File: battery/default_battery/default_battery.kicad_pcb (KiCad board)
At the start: 2 copper layers, 14 parts

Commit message: update battery module
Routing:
- net VBAT: track 31.0 -> 32.6 mm, vias 0 -> 1
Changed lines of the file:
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@@
 	)
 	(segment
-		(start -4.669 -35.494)
-		(end 1.874 -35.494)
-		(width 0.2)
-		(layer "F.Cu")
-		(net 1)
-	)
-	(segment
-		(start -5.175 -36)
-		(end -4.669 -35.494)
+		(start -5.175 -34.765)
+		(end -5.18 -34.76)
 		(width 0.2)
 		(layer "F.Cu")
@@
 	)
 	(segment
+		(start -5.175 -36)
+		(end -5.175 -34.765)
+		(width 0.2)
+		(layer "F.Cu")
+		(net 1)
+	)
+	(segment
 		(start 0 -26.54)
 		(end 2.54 -24)
@@
 		(net 1)
 	)
+	(via
+		(at -5.18 -34.76)
+		(size 0.6)
+		(drill 0.3)
+		(layers "F.Cu" "B.Cu")
+		(net 1)
+	)
+	(segment
+		(start 0 -33.64)
+		(end -1.12 -34.76)
+		(width 0.2)
+		(layer "B.Cu")
+		(net 1)
+	)
+	(segment
+		(start -1.12 -34.76)
+		(end -5.18 -34.76)
+		(width 0.2)
+		(layer "B.Cu")
+		(net 1)
+	)
+	(segment
+		(start 0 -31.62)
+		(end 0 -33.64)
+		(width 0.2)
+		(layer "B.Cu")
+		(net 1)
+	)

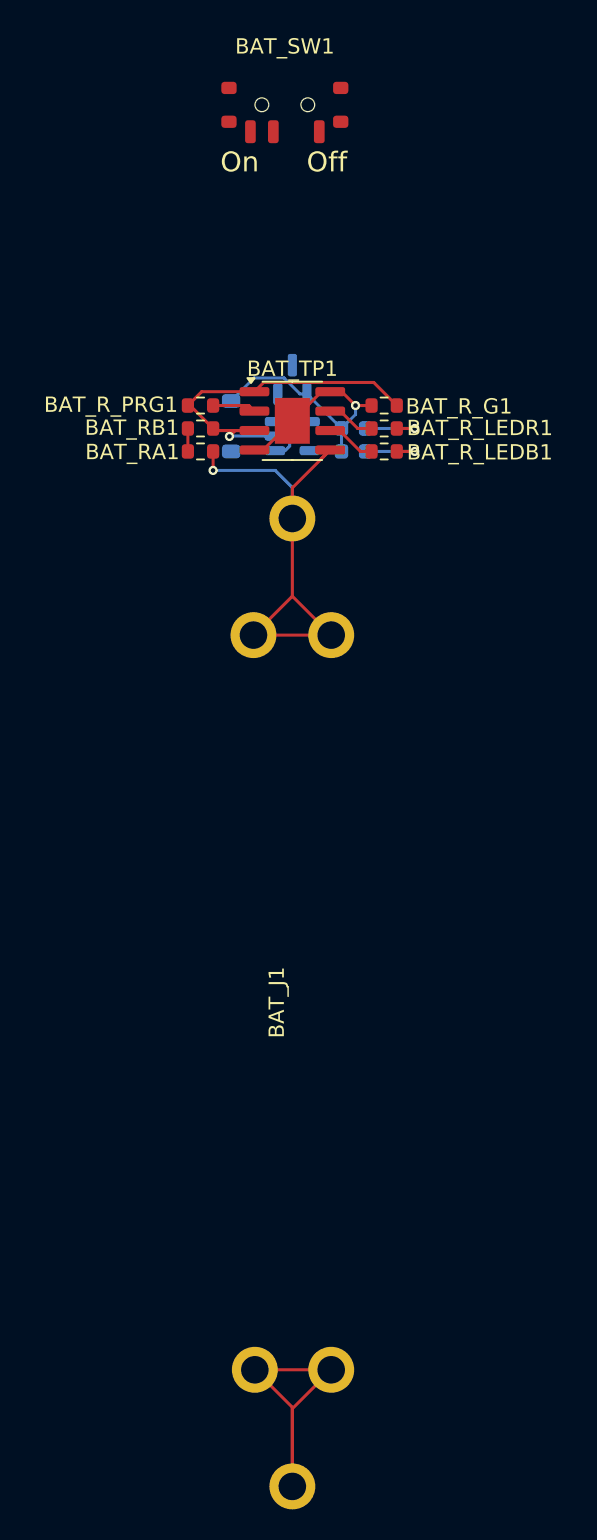
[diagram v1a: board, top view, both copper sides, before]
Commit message: update battery module, change switch
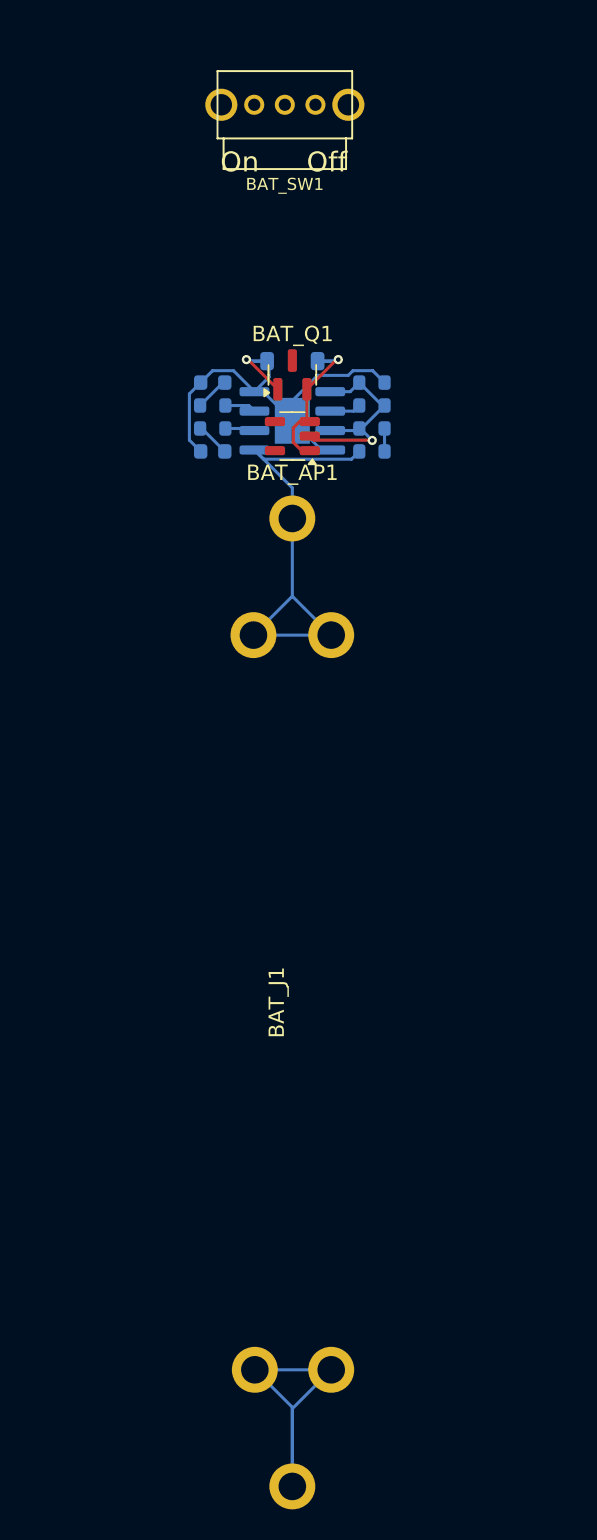
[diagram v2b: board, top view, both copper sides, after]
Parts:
- BAT_AP1, BAT_Q1: moved to F.Cu
- BAT_RA1, BAT_RB1, BAT_R_G1, BAT_R_LEDB1, BAT_R_LEDR1, BAT_R_PRG1, BAT_TP1: moved to B.Cu
- BAT_SW1: footprint ErgoCai.pretty:MSK-12C02 -> ErgoCai.pretty:SK12D07VG4
- moved BAT_R_LEDB1 11.3 mm to (-5.20, -37.5), turned to 0 degrees
- moved BAT_R_LEDR1 11.3 mm to (-5.20, -39.0), turned to 0 degrees
- moved BAT_RA1 11.2 mm to (5.20, -36.0), turned to 0 degrees
- moved BAT_RB1 11.2 mm to (5.20, -37.5), turned to 180 degrees
- moved BAT_R_PRG1 11.2 mm to (5.20, -39.0), turned to 0 degrees
- moved BAT_LEDR1 9.68 mm to (-5.20, -40.5)
- moved BAT_LEDB1 9.20 mm to (-5.20, -36.0)
- moved BAT_D1 5.84 mm to (0.00, -41.9), turned to 180 degrees
- moved BAT_R_G1 1.70 mm to (5.20, -40.5), turned to 180 degrees
- moved BAT_Q1 0.30 mm to (0.00, -41.0)
- turned BAT_AP1 to 180 degrees
- turned BAT_TP1 to 180 degrees
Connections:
- BAT_SW1 pad 1: unconnected-(BAT_SW1A-A-Pad1) -> Net-(BAT_Q1-D)
- BAT_SW1 pad 2: VBAT -> unconnected-(BAT_SW1-Pad2)
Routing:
- net GND: track 46.9 -> 36.4 mm
- net VBUS: track 23.0 -> 32.4 mm
- net Net-(BAT_AP1-EN): track 8.07 -> 11.2 mm, vias 0 -> 1
- net VBAT: track 32.6 -> 30.2 mm, vias 1 -> 0
- net Net-(BAT_LEDB1-K): track 4.45 -> 2.23 mm, vias 1 -> 0
- net Net-(BAT_LEDR1-K): track 4.44 -> 2.23 mm, vias 1 -> 0
- net Net-(BAT_TP1-~{STDBY}): track 3.07 -> 1.96 mm
- net Net-(BAT_TP1-~{CHRG}): track 2.97 -> 2.05 mm
- net Net-(BAT_TP1-PROG): track 2.65 -> 2.05 mm

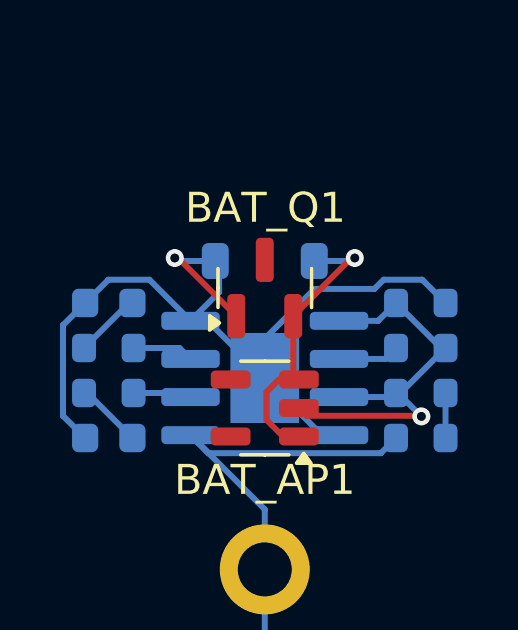
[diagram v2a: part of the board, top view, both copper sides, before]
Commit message: update battery module, update via pos
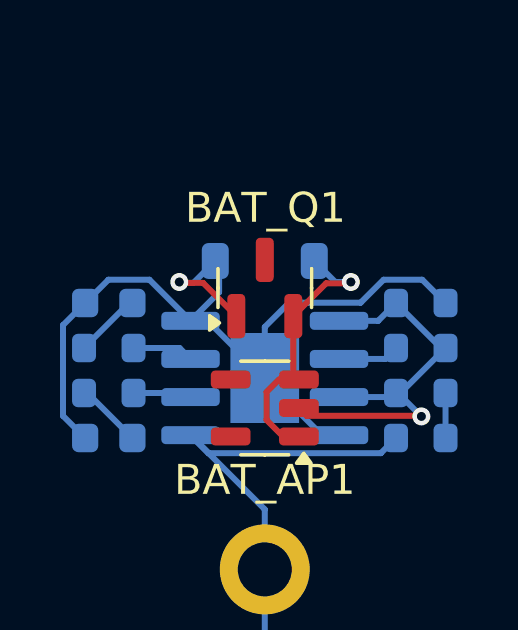
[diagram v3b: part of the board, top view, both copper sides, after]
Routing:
- net Net-(BAT_AP1-EN): track 11.2 -> 9.53 mm
- net VBUS: track 32.4 -> 30.9 mm
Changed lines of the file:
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@@
 	)
 	(segment
-		(start -2.8875 -42)
-		(end -3 -42)
+		(start -2.0575 -41.17)
+		(end -2.81 -41.17)
 		(width 0.2)
 		(layer "F.Cu")
@@
 	(segment
 		(start -0.95 -40.0625)
-		(end -2.8875 -42)
+		(end -2.0575 -41.17)
 		(width 0.2)
 		(layer "F.Cu")
@@
 	)
 	(via
-		(at -3 -42)
+		(at -2.85 -41.2)
 		(size 0.6)
 		(drill 0.3)
@@
 	)
 	(segment
+		(start -1.65 -41.9)
+		(end -2.38 -41.17)
+		(width 0.2)
+		(layer "B.Cu")
+		(net 4)
+	)
+	(segment
+		(start 3.961936 -41.276)
+		(end 5.249 -41.276)
+		(width 0.2)
+		(layer "B.Cu")
+		(net 4)
+	)
+	(segment
 		(start -6.726 -36.7385)
 		(end -6.726 -39.7615)
@@
 	)
 	(segment
-		(start -2.91 -41.9)
-		(end -2.92 -41.91)
-		(width 0.2)
-		(layer "B.Cu")
-		(net 4)
-	)
-	(segment
 		(start -5.9875 -36)
 		(end -6.726 -36.7385)
@@
 	)
 	(segment
-		(start 0 -39.310761)
-		(end 1.658239 -40.969)
+		(start 3.195936 -40.51)
+		(end 3.961936 -41.276)
 		(width 0.2)
 		(layer "B.Cu")
@@
 	)
 	(segment
+		(start 0 -38)
+		(end 0 -39.7)
+		(width 0.2)
+		(layer "B.Cu")
+		(net 4)
+	)
+	(segment
 		(start -5.2115 -41.276)
 		(end -3.846 -41.276)
@@
 	)
 	(segment
+		(start 5.249 -41.276)
+		(end 6.025 -40.5)
+		(width 0.2)
+		(layer "B.Cu")
+		(net 4)
+	)
+	(segment
 		(start -6.726 -39.7615)
 		(end -5.9875 -40.5)
@@
 	)
 	(segment
-		(start 3.654936 -40.969)
-		(end 3.961936 -41.276)
-		(width 0.2)
-		(layer "B.Cu")
-		(net 4)
-	)
-	(segment
-		(start -2.9 -41.9)
-		(end -3 -42)
+		(start 0 -39.7)
+		(end 0.81 -40.51)
 		(width 0.2)
 		(layer "B.Cu")
@@
 	)
 	(segment
-		(start -1.65 -41.9)
-		(end -2.9 -41.9)
-		(width 0.2)
-		(layer "B.Cu")
-		(net 4)
-	)
-	(segment
 		(start -1.5225 -40.8575)
 		(end -1.5225 -41.87)
@@
 	)
 	(segment
-		(start 3.961936 -41.276)
-		(end 5.249 -41.276)
-		(width 0.2)
-		(layer "B.Cu")
-		(net 4)
-	)
-	(segment
 		(start 0 -38)
 		(end 1.905 -36.095)
@@
 	)
 	(segment
-		(start -2.73 -41.9)
-		(end -2.91 -41.9)
-		(width 0.2)
-		(layer "B.Cu")
-		(net 4)
-	)
-	(segment
-		(start 5.249 -41.276)
-		(end 6.025 -40.5)
-		(width 0.2)
-		(layer "B.Cu")
-		(net 4)
-	)
-	(segment
 		(start -5.9875 -40.5)
 		(end -5.2115 -41.276)
@@
 	)
 	(segment
-		(start -1.65 -41.9)
-		(end -2.73 -41.9)
-		(width 0.2)
-		(layer "B.Cu")
-		(net 4)
-	)
-	(segment
-		(start 1.658239 -40.969)
-		(end 3.654936 -40.969)
-		(width 0.2)
-		(layer "B.Cu")
-		(net 4)
-	)
-	(segment
-		(start 0 -38)
-		(end 0 -39.310761)
-		(width 0.2)
-		(layer "B.Cu")
-		(net 4)
-	)
-	(segment
-		(start 2.8875 -42)
-		(end 3 -42)
+		(start 0.81 -40.51)
+		(end 3.195936 -40.51)
+		(width 0.2)
+		(layer "B.Cu")
+		(net 4)
+	)
+	(segment
+		(start -2.38 -41.17)
+		(end -2.81 -41.17)
+		(width 0.2)
+		(layer "B.Cu")
+		(net 4)
+	)
+	(segment
+		(start 0.95 -40.0625)
+		(end 2.0435 -41.156)
 		(width 0.2)
 		(layer "F.Cu")
@@
 	)
 	(segment
+		(start 2.0435 -41.156)
+		(end 2.84 -41.156)
+		(width 0.2)
+		(layer "F.Cu")
+		(net 7)
+	)
+	(segment
 		(start 0.61 -36.05)
 		(end 1.1375 -36.05)
@@
 		(net 7)
 	)
-	(segment
-		(start 0.95 -40.0625)
-		(end 2.8875 -42)
-		(width 0.2)
-		(layer "F.Cu")
-		(net 7)
-	)
 	(via
-		(at 3 -42)
+		(at 2.87 -41.2)
 		(size 0.6)
 		(drill 0.3)
@@
 	)
 	(segment
-		(start 1.65 -41.9)
-		(end 2.9 -41.9)
-		(width 0.2)
-		(layer "B.Cu")
-		(net 7)
-	)
-	(segment
-		(start 2.9 -41.9)
-		(end 3 -42)
-		(width 0.2)
-		(layer "B.Cu")
-		(net 7)
-	)
-	(segment
-		(start 2.8 -41.9)
-		(end 2.81 -41.91)
-		(width 0.2)
-		(layer "B.Cu")
-		(net 7)
-	)
-	(segment
-		(start 2.81 -41.91)
-		(end 2.93 -41.91)
-		(width 0.2)
-		(layer "B.Cu")
-		(net 7)
-	)
-	(segment
-		(start 1.65 -41.9)
-		(end 2.8 -41.9)
-		(width 0.2)
-		(layer "B.Cu")
-		(net 7)
-	)
-	(segment
-		(start 2.93 -41.91)
-		(end 2.94 -41.92)
-		(width 0.2)
-		(layer "B.Cu")
+		(start 2.87 -41.2)
+		(end 2.35 -41.2)
+		(width 0.2)
+		(layer "B.Cu")
+		(net 7)
+	)
+	(segment
+		(start 2.35 -41.2)
+		(end 1.65 -41.9)
+		(width 0.2)
+		(layer "B.Cu")

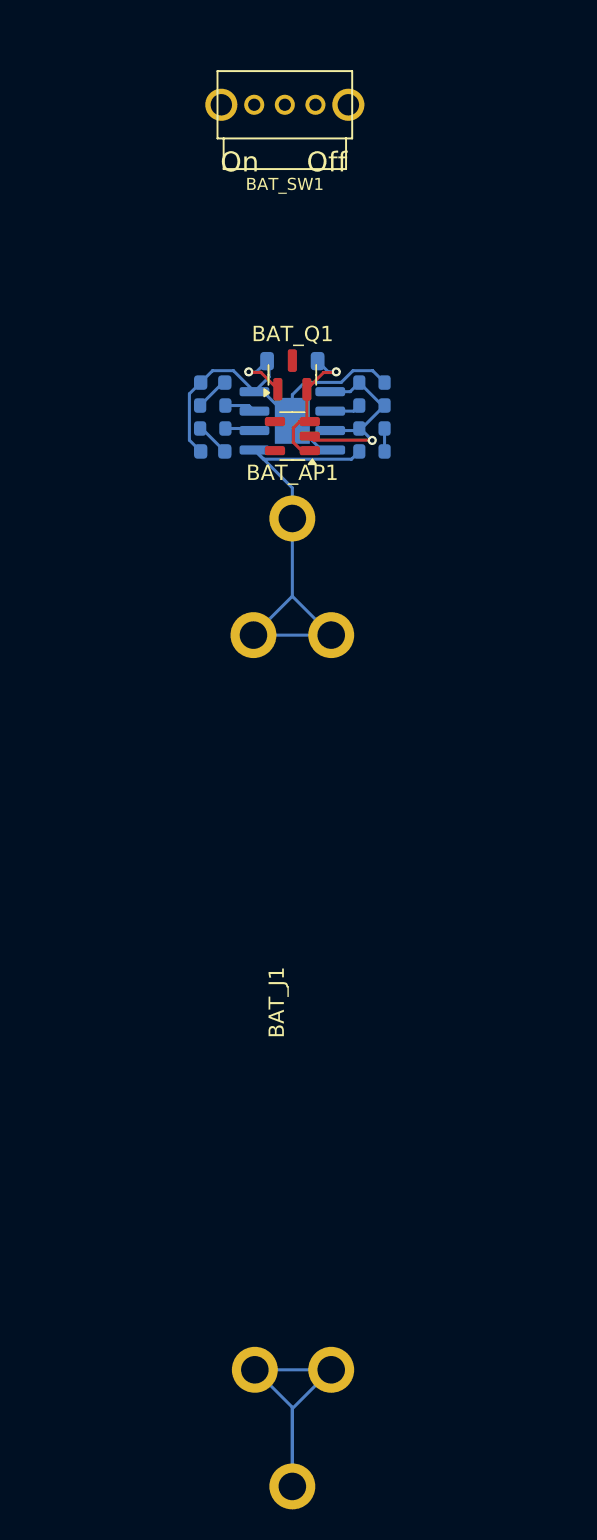
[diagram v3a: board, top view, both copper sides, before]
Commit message: move tp4056 to front
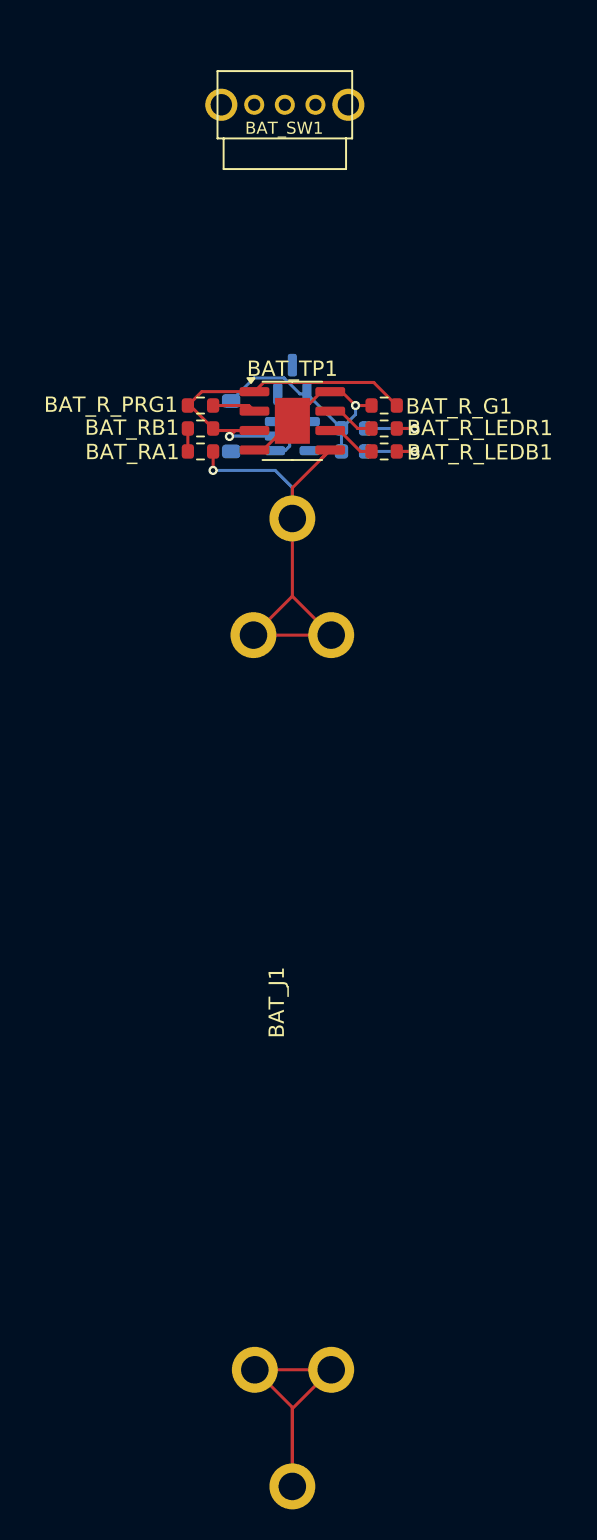
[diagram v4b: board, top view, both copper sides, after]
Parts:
- BAT_AP1, BAT_Q1: moved to B.Cu
- BAT_RA1, BAT_RB1, BAT_R_G1, BAT_R_LEDB1, BAT_R_LEDR1, BAT_R_PRG1, BAT_TP1: moved to F.Cu
- moved BAT_R_LEDB1 11.3 mm to (6.00, -36.0), turned to 180 degrees
- moved BAT_R_LEDR1 11.3 mm to (6.00, -37.5), turned to 180 degrees
- moved BAT_RA1 11.2 mm to (-6.00, -36.0), turned to 180 degrees
- moved BAT_RB1 11.2 mm to (-6.00, -37.5), turned to 0 degrees
- moved BAT_R_PRG1 11.2 mm to (-6.00, -39.0), turned to 180 degrees
- moved BAT_LEDR1 9.68 mm to (4.00, -37.5)
- moved BAT_LEDB1 9.20 mm to (4.00, -36.0)
- moved BAT_D1 5.84 mm to (-4.00, -37.6), turned to 90 degrees
- moved BAT_R_G1 1.70 mm to (6.00, -39.0), turned to 0 degrees
- moved BAT_Q1 0.30 mm to (0.00, -40.7)
- turned BAT_AP1 to 0 degrees
- turned BAT_TP1 to 0 degrees
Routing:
- net GND: track 36.4 -> 46.9 mm
- net VBUS: track 30.9 -> 23.0 mm
- net VBAT: track 30.2 -> 32.6 mm, vias 0 -> 1
- net Net-(BAT_LEDB1-K): track 2.23 -> 4.45 mm, vias 0 -> 1
- net Net-(BAT_LEDR1-K): track 2.23 -> 4.44 mm, vias 0 -> 1
- net Net-(BAT_AP1-EN): track 9.53 -> 8.07 mm, vias 1 -> 0
- net Net-(BAT_TP1-~{STDBY}): track 1.96 -> 3.07 mm
- net Net-(BAT_TP1-~{CHRG}): track 2.05 -> 2.97 mm
- net Net-(BAT_TP1-PROG): track 2.05 -> 2.65 mm

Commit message: mvoe battery led to front
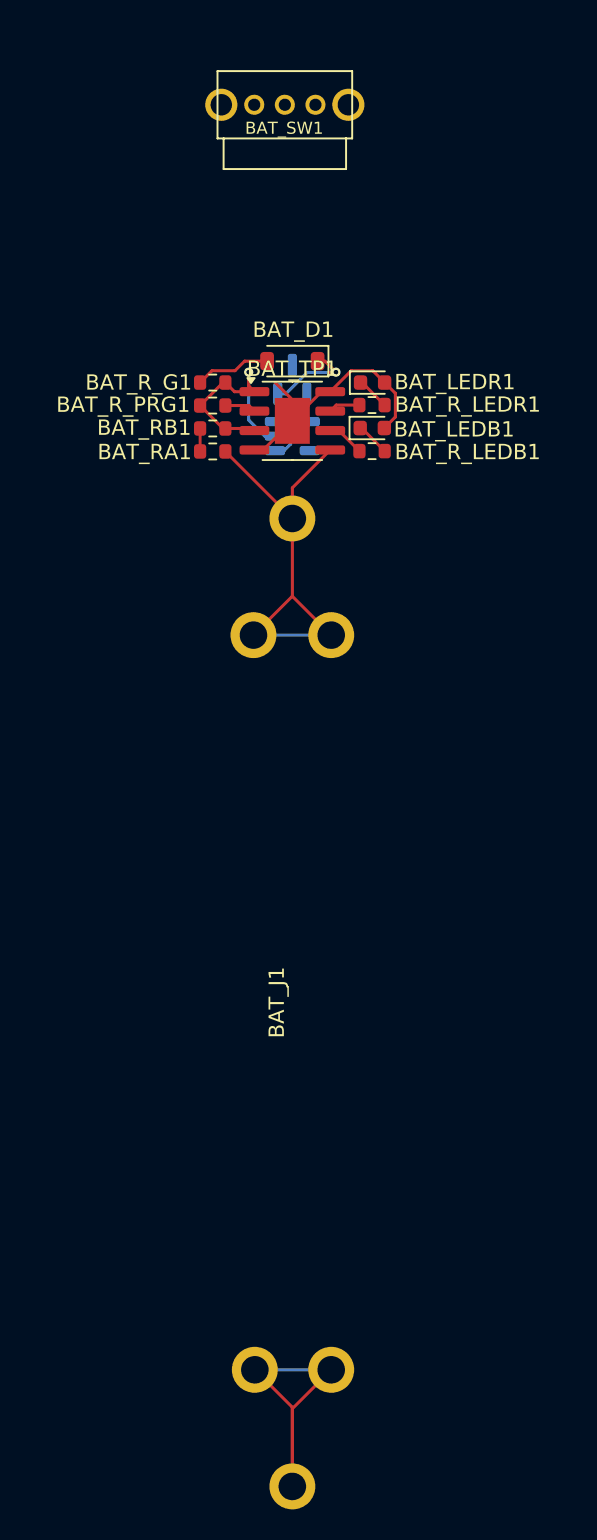
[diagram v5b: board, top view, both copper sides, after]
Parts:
- BAT_D1, BAT_LEDB1, BAT_LEDR1: moved to F.Cu
- moved BAT_R_G1 11.3 mm to (-5.20, -40.5)
- moved BAT_D1 5.84 mm to (0.00, -41.9), turned to 180 degrees
- moved BAT_LEDR1 3.25 mm to (5.24, -40.5), turned to 0 degrees
- moved BAT_LEDB1 1.96 mm to (5.22, -37.5), turned to 0 degrees
- moved BAT_R_LEDR1 1.72 mm to (5.21, -39.0)
- moved BAT_RA1 0.80 mm to (-5.20, -36.0)
- moved BAT_RB1 0.80 mm to (-5.20, -37.5)
- moved BAT_R_PRG1 0.80 mm to (-5.20, -39.0)
- moved BAT_R_LEDB1 0.79 mm to (5.21, -36.0)
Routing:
- net GND: track 46.9 -> 37.8 mm
- net Net-(BAT_AP1-EN): track 8.07 -> 11.7 mm, vias 0 -> 1
- net VBAT: track 32.6 -> 29.0 mm, vias 1 -> 0
- net Net-(BAT_LEDR1-K): track 4.44 -> 2.18 mm, vias 1 -> 0
- net Net-(BAT_LEDB1-K): track 4.45 -> 2.23 mm, vias 1 -> 0
- net Net-(BAT_TP1-~{CHRG}): track 2.97 -> 2.07 mm
- net Net-(BAT_TP1-PROG): track 2.65 -> 2.05 mm
- net Net-(BAT_TP1-~{STDBY}): track 3.07 -> 2.47 mm
- net VBUS: track 23.0 -> 22.5 mm, vias 1 -> 0
